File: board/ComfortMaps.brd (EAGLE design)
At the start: 96.8 x 49.3 mm, 47 parts, among them J1 PROG_HDR, U1 ADXL362, U3 ADP160-3.3, U4 MCP73833, X1 RASPI_GPIO_B+#_PIN

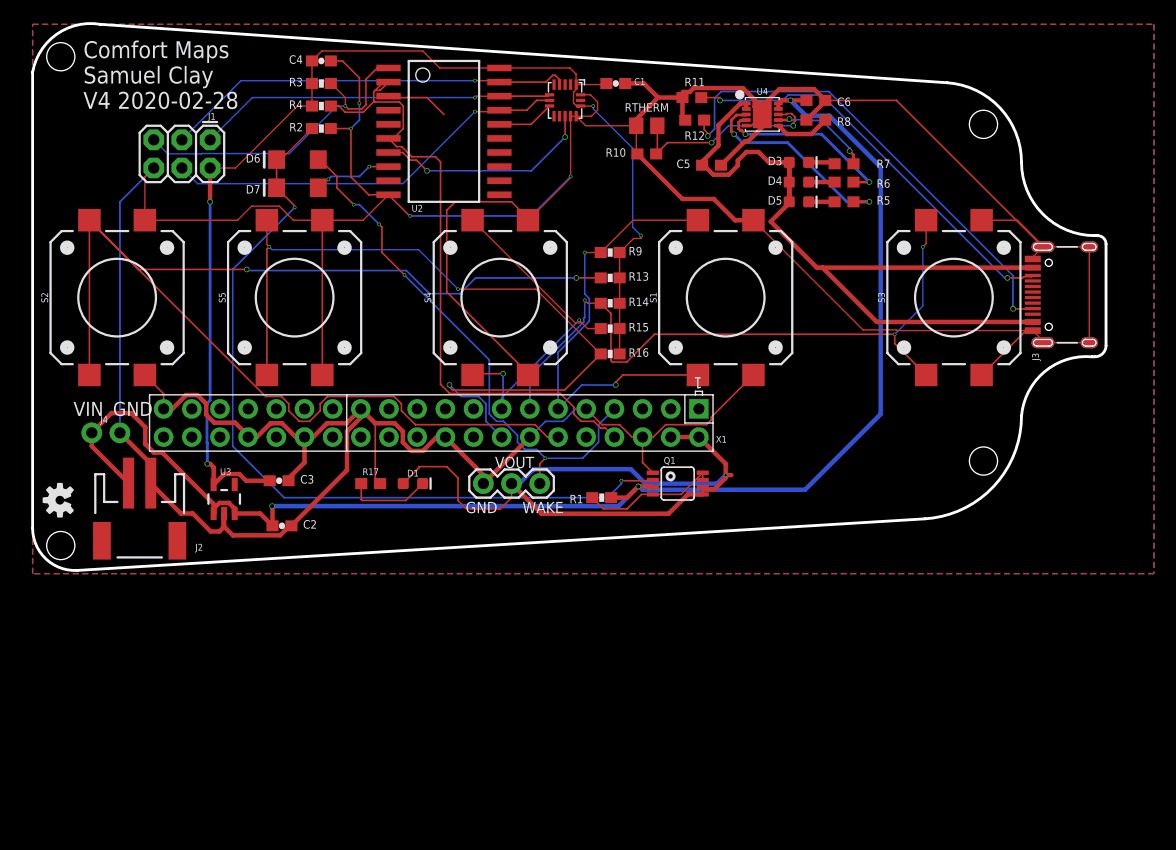
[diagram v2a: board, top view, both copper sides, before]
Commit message: v4 of the PCB. Moved around components for better soldering, added Wake/override led, pulldown on wake.
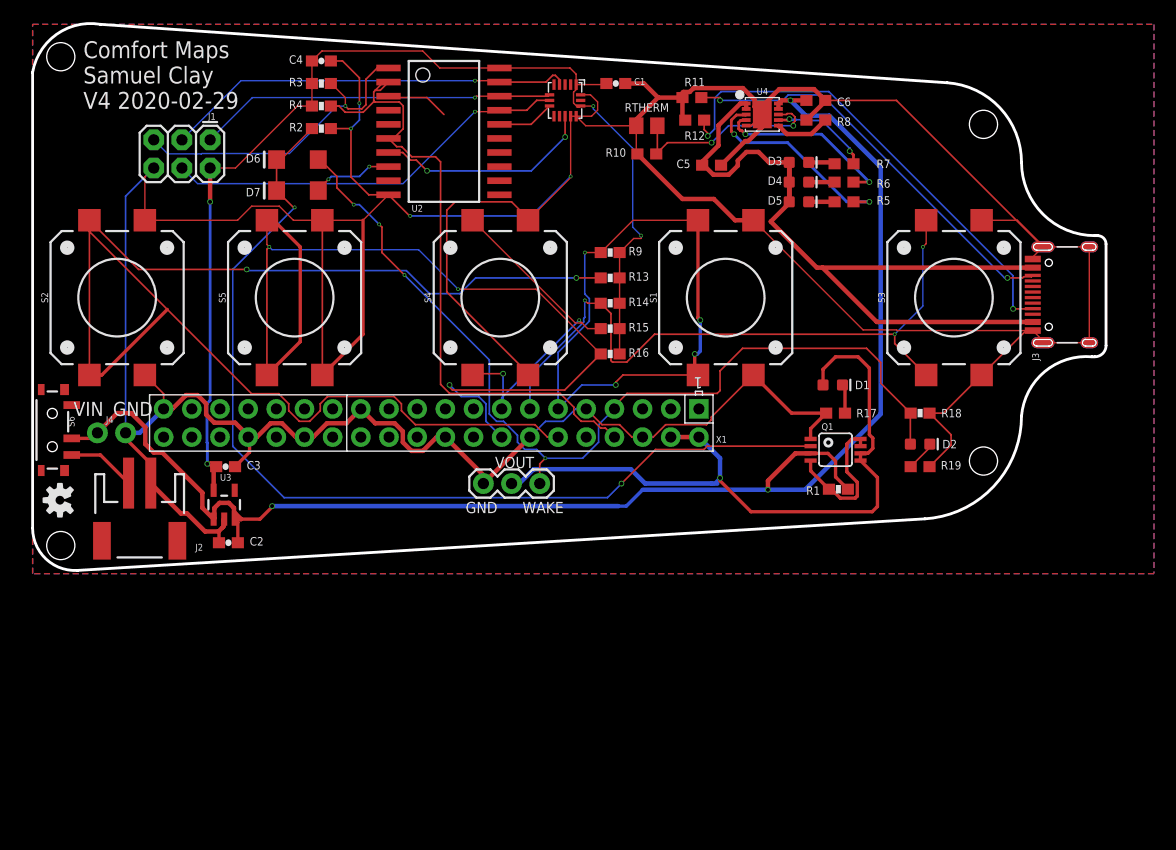
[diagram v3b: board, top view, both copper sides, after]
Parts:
- added D2: RED, SparkFun-LED:LED-0603
- added R18: 10k, SparkFun-Resistors:0603-RES
- added R19: 1.5k, SparkFun-Resistors:0603
- added S6: (no value), SparkFun-Switches:SWITCH_SPST_SMD_A
- moved R17 42.4 mm to (76.2, 8.13), turned to 180 degrees
- moved D1 38.9 mm to (75.9, 10.7)
- moved R1 21.3 mm to (76.5, 1.27)
- moved Q1 14.5 mm to (76.2, 4.83)
- moved C2 5.06 mm to (21.5, -3.56), turned to 180 degrees
- moved C3 4.99 mm to (21.2, 3.30)
- moved U3 0.51 mm to (21.1, -0.13)
- moved J4 0.51 mm to (9.65, 6.35)
- moved D7 0.25 mm to (27.7, 28.2)
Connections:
- new net N$15: J2.2, S6.1
- new net N$16: D2.C, R19.1
- net GND: now also R18.2, R19.2
- net OVERRIDE: now also D2.A, R18.1
- net V_BATT: now also S6.2; no longer J2.2
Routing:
- net OVERRIDE: track 48.3 -> 84.7 mm
- net GPIO23: track 70.9 -> 87.6 mm
- net N$2: track 74.2 -> 89.6 mm
- net GPIO17: track 40.9 -> 55.4 mm, vias 2 -> 4
- net GND: track 419.3 -> 431.6 mm
- net GPIO18: track 116.7 -> 126.7 mm
- net N$15: track 0.00 -> 6.17 mm
- net V_BATT: track 130.5 -> 136.3 mm
- net N$14: track 7.64 -> 2.63 mm
- net 3.3V: track 108.2 -> 103.2 mm
- net N$16: track 0.00 -> 2.75 mm
- net VOUT: track 66.2 -> 64.0 mm
- net N$1: track 12.4 -> 13.4 mm
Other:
- board text added: "Comfort Maps Samuel Clay V4 2020-02-29"
- board text removed: "Comfort Maps Samuel Clay V4 2020-02-28"

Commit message: Finalizing v4 of board. Moving battery connector so the entire 40 pin connector is solderable and the battery wire no longer gets stuck.
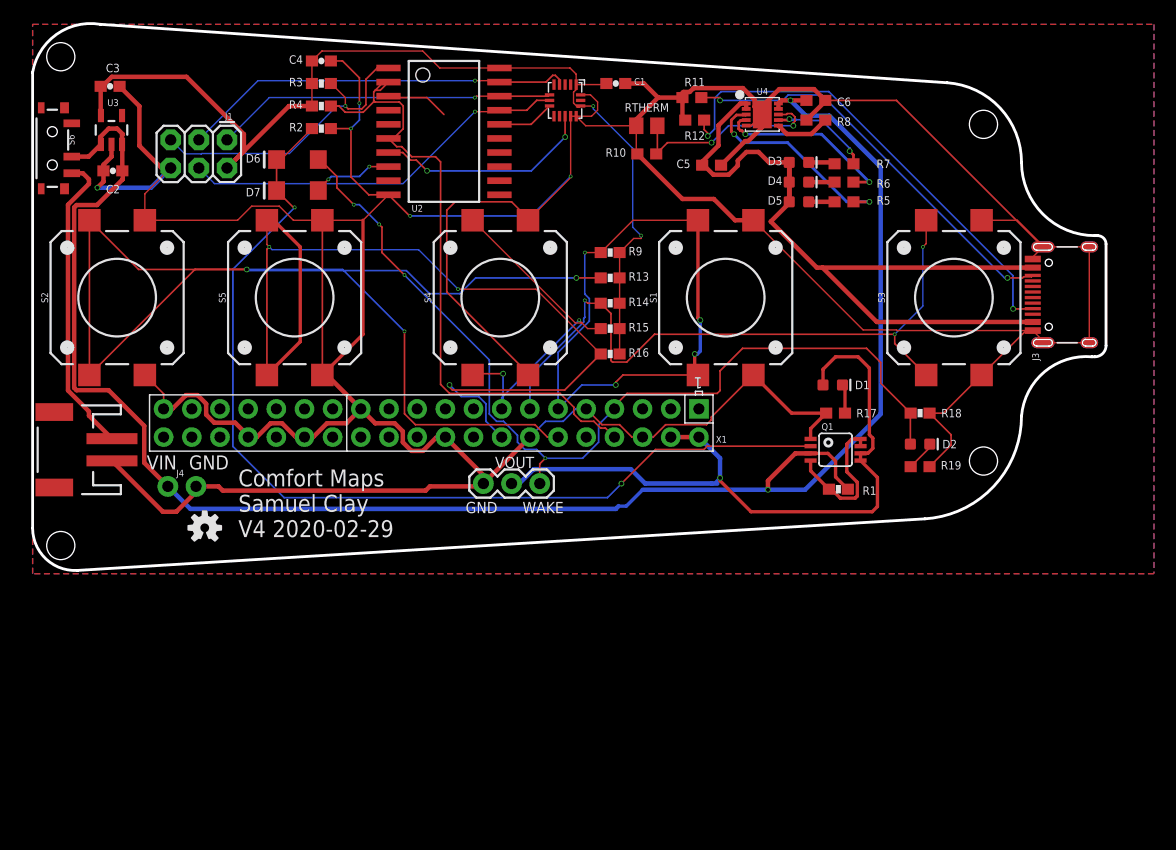
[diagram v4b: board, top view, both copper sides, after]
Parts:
- moved C3 35.8 mm to (10.8, 37.6)
- moved U3 35.3 mm to (10.9, 33.7)
- moved C2 35.1 mm to (11.0, 30.0)
- moved S6 25.4 mm to (5.59, 32.0)
- moved U$3 13.3 mm to (19.3, -2.21), turned to 0 degrees
- moved J2 9.13 mm to (7.26, 4.83), turned to 90 degrees
- moved J4 7.98 mm to (16.0, 1.52)
- moved J1 1.52 mm to (21.3, 32.8)
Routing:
- net V_BATT: track 136.3 -> 162.1 mm, vias 3 -> 2
- net N$15: track 6.17 -> 27.6 mm
- net GND: track 431.6 -> 446.8 mm, vias 4 -> 5
- net 3.3V: track 103.2 -> 93.6 mm, vias 4 -> 2
- net GPIO18: track 126.7 -> 120.2 mm, vias 2 -> 3
- net SCK: track 37.8 -> 36.2 mm
- net RESET: track 29.0 -> 27.5 mm
- net MOSI: track 36.9 -> 35.4 mm
- net MISO: track 32.9 -> 31.3 mm

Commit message: V5 board, with new usb type c connector and lipo charge controller.
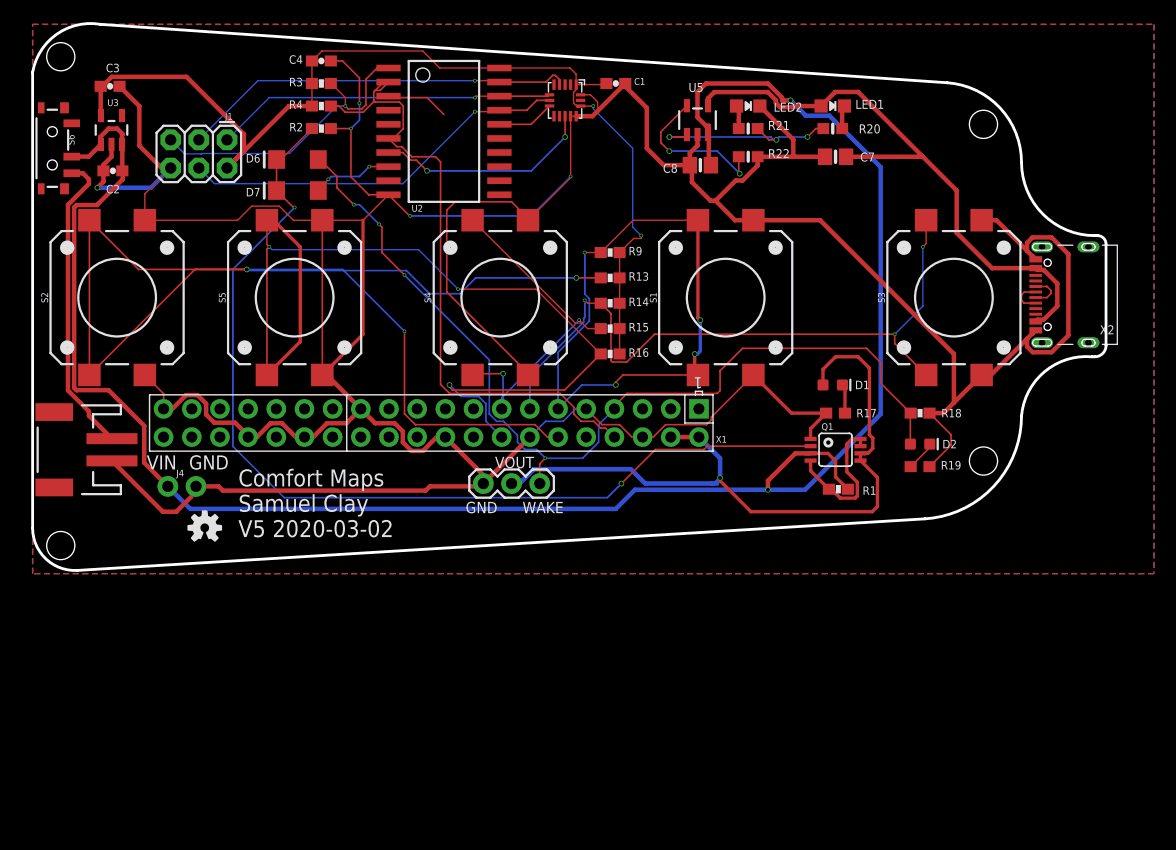
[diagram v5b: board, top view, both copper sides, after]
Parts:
- removed C5, C6: 10uF, SparkFun-Capacitors:0603
- removed D3: RED, SparkFun-LED:LED-0603
- removed D4: GREEN, SparkFun-LED:LED-0603
- removed D5: Yellow, SparkFun-LED:LED-0603
- removed J3: (no value), SparkFun-Connectors:USB-C-16P
- removed R10: 10k, SparkFun-Resistors:0603
- removed R11, R12: 5.1k, SparkFun-Resistors:0603
- removed R5, R6, R7: 1.5k, SparkFun-Resistors:0603
- removed R8: 1k, SparkFun-Resistors:0603
- removed RTHERM: THERM, resistor:R0805
- removed U4: MCP73833, SparkFun-IC-Power:DFN-10
- added C7, C8: 10µF, microbuilder:0805-NO@1
- added LED1: RED, microbuilder:CHIPLED_0805_NOOUTLINE
- added LED2: GREEN, microbuilder:CHIPLED_0805_NOOUTLINE
- added R20, R21: 470, microbuilder:0603-NO
- added R22: 2.2K, microbuilder:0603-NO
- added U5: MCP73831T-2ACI/OT, microbuilder:SOT23-5
- added X2: (no value), microbuilder:USB_C_CUSB31-CFM2AX-01-X
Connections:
- removed net N$10: D4.C, R6.1
- removed net N$11: D5.C, R5.1
- removed net N$12: J3.B5, R11.2
- removed net N$13: J3.A5, R12.2
- removed net N$9: D3.C, R7.1
- removed net PG: R7.2, U4.P$7
- removed net PROG: R8.2, U4.P$6
- removed net STAT1: R5.2, U4.P$3
- removed net STAT2: R6.2, U4.P$4
- removed net THERM: R10.2, RTHERM.2, U4.P$8
- new net CC1: X2.A5
- new net CC2: X2.B5
- new net D+: X2.A6, X2.B6
- new net D-: X2.A7, X2.B7
- new net N$17: LED1.C, R20.1
- new net N$18: R20.2, R21.2, U5.1
- new net N$19: R22.1, U5.5
- new net N$20: LED2.A, R21.1
- net GND: now also C7.2, C8.2, LED2.C, R22.2, U5.2, X2.A1B12, X2.B1A12; no longer C5.2, C6.2, J3.GND, J3.GND2, J3.SHLD1, J3.SHLD2, J3.SHLD3, J3.SHLD4, J3.SHLD5, J3.SHLD6, J3.SHLD7, J3.SHLD8, R10.1, R11.1, R12.1, R8.1, RTHERM.1, U4.P$11, U4.P$5
- net V_BATT: now also C8.1, U5.3; no longer C6.1, U4.P$10, U4.P$9
- net V_USB: now also C7.1, LED1.A, U5.4, X2.A4B9, X2.B4A9; no longer C5.1, D3.A, D4.A, D5.A, J3.VBUS1, J3.VBUS2, U4.P$1, U4.P$2
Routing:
- net N$13: track 44.1 -> 0.00 mm, vias 2 -> 0
- net GND: track 446.8 -> 404.7 mm
- net N$12: track 37.3 -> 0.00 mm, vias 2 -> 0
- net V_USB: track 73.6 -> 54.5 mm
- net STAT1: track 19.1 -> 0.00 mm, vias 2 -> 0
- net THERM: track 18.5 -> 0.00 mm, vias 2 -> 0
- net N$18: track 0.00 -> 18.2 mm, vias 0 -> 3
- net STAT2: track 16.6 -> 0.00 mm, vias 2 -> 0
- net N$19: track 0.00 -> 14.1 mm, vias 0 -> 2
- net V_BATT: track 162.1 -> 175.8 mm
- net PG: track 9.16 -> 0.00 mm, vias 2 -> 0
- net PROG: track 5.09 -> 0.00 mm
- net D+: track 0.00 -> 3.35 mm
- net D-: track 0.00 -> 3.27 mm
- net N$9: track 2.39 -> 0.00 mm
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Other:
- board text added: "Comfort Maps Samuel Clay V5 2020-03-02"
- board text removed: "Comfort Maps Samuel Clay V4 2020-02-29"

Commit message: V5
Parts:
- S6: value (none) -> MA12RTR
- U2: value (none) -> ATTINY2313
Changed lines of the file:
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@@
 <?xml version="1.0" encoding="utf-8"?>
 <!DOCTYPE eagle SYSTEM "eagle.dtd">
-<eagle version="9.5.1">
+<eagle version="9.5.2">
 <drawing>
 <settings>
@@
 <attribute name="VALUE" x="19.812" y="34.925" size="0.6096" layer="27" ratio="20" rot="R180"/>
 </element>
-<element name="U2" library="SparkFun-DigitalIC" package="SOP20W" value="" x="40.894" y="33.528" smashed="yes" rot="R270">
+<element name="U2" library="SparkFun-DigitalIC" package="SOP20W" value="ATTINY2313" x="40.894" y="33.528" smashed="yes" rot="R270">
 <attribute name="DIST" value="DIGIKEY" x="40.894" y="33.528" size="1.778" layer="27" rot="R270" display="off"/>
 <attribute name="DIST_ID" value="ATTINY2313A-SU-ND" x="40.894" y="33.528" size="1.778" layer="27" rot="R270" display="off"/>
@@
 <attribute name="VALUE" x="76.2" y="8.89" size="0.6096" layer="27" font="vector" ratio="20" rot="R180" align="top-center"/>
 </element>
-<element name="S6" library="SparkFun-Switches" library_urn="urn:adsk.eagle:library:535" package="SWITCH_SPST_SMD_A" package3d_urn="urn:adsk.eagle:package:40179/1" value="" x="5.588" y="32.004" smashed="yes" rot="R90">
+<element name="S6" library="SparkFun-Switches" library_urn="urn:adsk.eagle:library:535" package="SWITCH_SPST_SMD_A" package3d_urn="urn:adsk.eagle:package:40179/1" value="MA12RTR" x="5.588" y="32.004" smashed="yes" rot="R90">
+<attribute name="DIGIKEY" value="679-1847-1-ND" x="5.588" y="32.004" size="1.778" layer="27" rot="R90" display="off"/>
 <attribute name="NAME" x="6.985" y="32.766" size="0.6096" layer="25" font="vector" ratio="20" rot="R270" align="bottom-center"/>
 <attribute name="PROD_ID" value="SWCH-10651" x="5.588" y="32.004" size="1.778" layer="27" rot="R90" display="off"/>

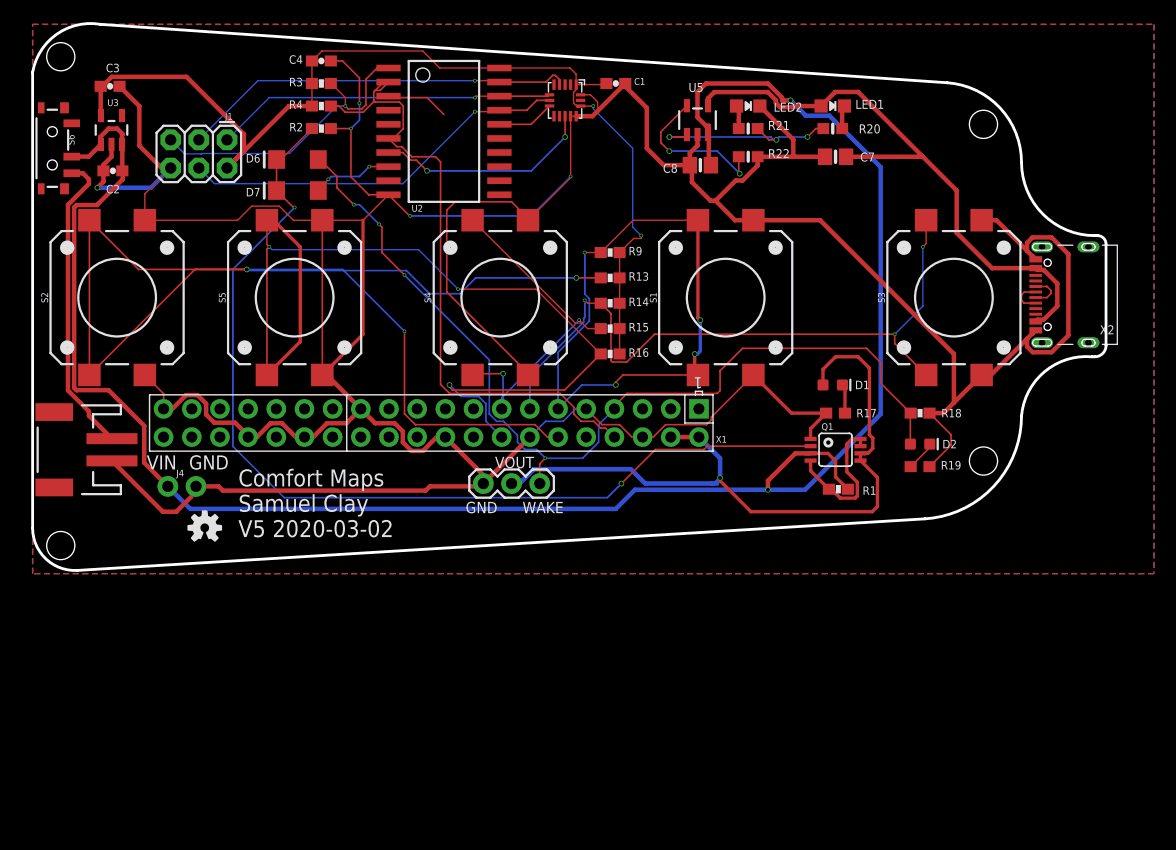
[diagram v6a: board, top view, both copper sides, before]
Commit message: Moving back to older lipo charger.
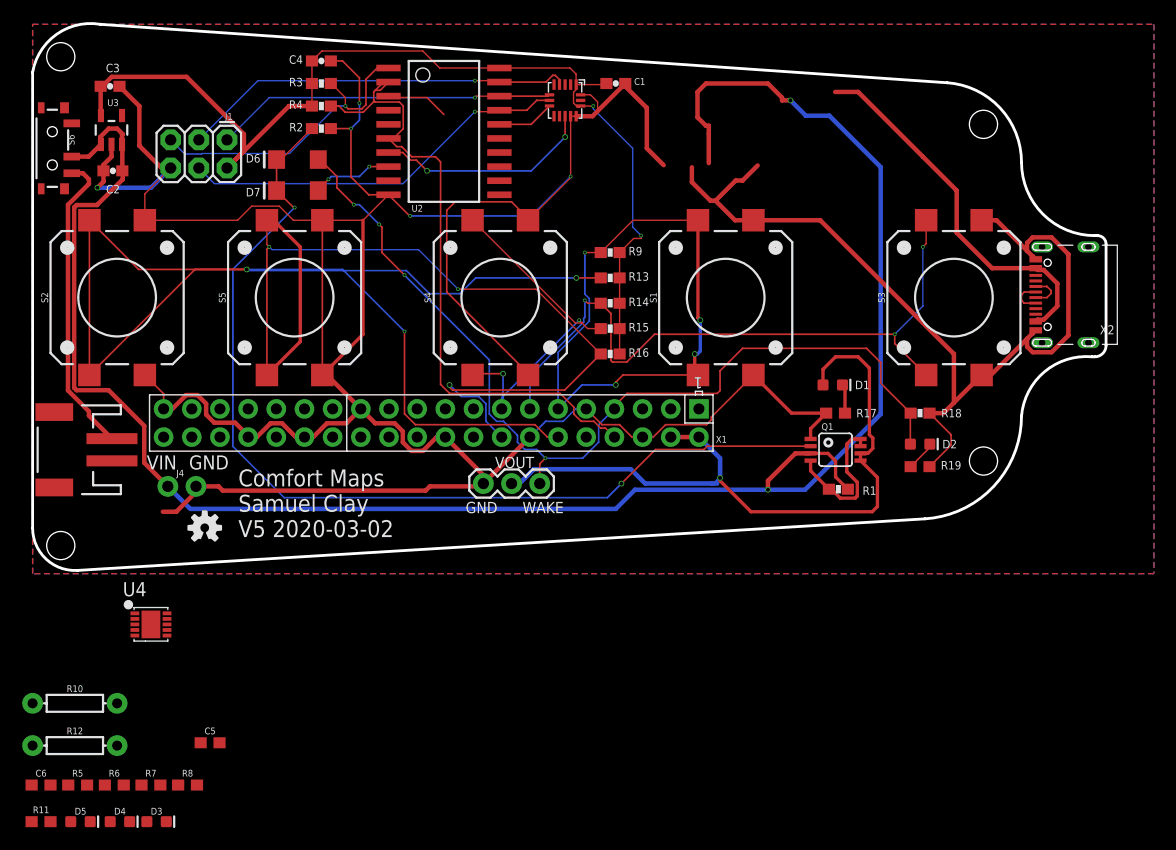
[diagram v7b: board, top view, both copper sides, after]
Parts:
- removed C7, C8: 10µF, microbuilder:0805-NO@1
- removed LED1: RED, microbuilder:CHIPLED_0805_NOOUTLINE
- removed LED2: GREEN, microbuilder:CHIPLED_0805_NOOUTLINE
- removed R20, R21: 470, microbuilder:0603-NO
- removed R22: 2.2K, microbuilder:0603-NO
- removed U5: MCP73831T-2ACI/OT, microbuilder:SOT23-5
- added C5, C6: 10uF, SparkFun-Capacitors:0603
- added D3: RED, SparkFun-LED:LED-0603
- added D4: GREEN, SparkFun-LED:LED-0603
- added D5: Yellow, SparkFun-LED:LED-0603
- added R10: THERM, SparkFun-Resistors:AXIAL-0.3
- added R11: 10k, SparkFun-Resistors:0603
- added R12: 1k, SparkFun-Resistors:AXIAL-0.3
- added R5, R6, R7: 1.5k, SparkFun-Resistors:0603
- added R8: 1k, SparkFun-Resistors:0603
- added U4: MCP73833, SparkFun-IC-Power:DFN-10
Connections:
- removed net N$17: LED1.C, R20.1
- removed net N$18: R20.2, R21.2, U5.1
- removed net N$19: R22.1, U5.5
- removed net N$20: LED2.A, R21.1
- removed net V_USB: C7.1, LED1.A, U5.4, X2.A4B9, X2.B4A9
- new net N$11: D4.C, R6.1
- new net N$12: D5.C, R5.1
- new net N$9: D3.C, R7.1
- new net PG: R7.2, U4.P$7
- new net PROG: R12.P$2, R8.2, U4.P$6
- new net STAT1: R5.2, U4.P$3
- new net STAT2: R6.2, U4.P$4
- new net THERM: R10.P$2, R11.2, U4.P$8
- new net VDD: C5.1, D3.A, D4.A, D5.A, U4.P$1, U4.P$2, X2.A4B9, X2.B4A9
- net GND: now also C5.2, C6.2, R10.P$1, R11.1, R12.P$1, R8.1, U4.P$11, U4.P$5; no longer C7.2, C8.2, LED2.C, R22.2, U5.2
- net V_BATT: now also C6.1, U4.P$10, U4.P$9; no longer C8.1, U5.3
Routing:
- net V_USB: track 54.5 -> 0.00 mm
- net VDD: track 0.00 -> 34.0 mm
- net GND: track 404.7 -> 379.8 mm
- net N$18: track 18.2 -> 0.00 mm, vias 3 -> 0
- net N$19: track 14.1 -> 0.00 mm, vias 2 -> 0
- net N$20: track 2.11 -> 0.00 mm
- net N$17: track 2.11 -> 0.00 mm
